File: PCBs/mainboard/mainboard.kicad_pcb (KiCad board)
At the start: 2 copper layers, 76.6 x 80 mm, 32 parts, among them J1 USB_C_Receptacle_USB2.0_16P, SW1 SW_Push_Dual, SW2 SW_Push_Dual, SW3 SW_Push_Dual, U3 ESP32-S3-WROOM-1

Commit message: Layouting pt.1
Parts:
- moved D5 76.5 mm to (83.2, 134.1)
- moved R3 74.3 mm to (83.2, 132.1), turned to 180 degrees
- moved D3 73.5 mm to (60.6, 109.9), turned to 135 degrees
- moved D4 72.3 mm to (60.6, 108.0), turned to -135 degrees
- moved C8 72.1 mm to (82.8, 77.7), turned to -45 degrees
- moved C3 71.2 mm to (83.2, 129.7), turned to 180 degrees
- moved R1 71.2 mm to (61.8, 106.1), turned to 0 degrees
- moved C2 70.5 mm to (83.8, 121.1), turned to 0 degrees
- moved R2 70.4 mm to (62.7, 112.0)
- moved D2 70.3 mm to (60.5, 112.1), turned to 135 degrees
- moved R8 69.8 mm to (61.8, 103.7), turned to 0 degrees
- moved U4 69.1 mm to (82.9, 125.2), turned to 0 degrees
- moved D1 68.9 mm to (63.3, 115.5)
- moved U2 68.7 mm to (109.5, 132.7)
- moved R6 68.4 mm to (82.1, 74.1), turned to 90 degrees
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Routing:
- net VCC_3V3: track 30.8 -> 229.9 mm, vias 0 -> 3
- net GPIO16: track 6.50 -> 63.2 mm, vias 0 -> 1
- net ESP_3V3: track 11.7 -> 54.8 mm, vias 0 -> 2
- net D-: track 0.00 -> 42.2 mm
- net D+: track 0.00 -> 41.3 mm
- net VCC_4V5: track 15.0 -> 45.9 mm, vias 0 -> 1
- net CHIP_PU: track 33.2 -> 46.1 mm, vias 0 -> 2
- net Net-(D1-A): track 0.00 -> 12.0 mm
- net VCC_5V: track 3.37 -> 14.2 mm
- net GPIO37: track 93.5 -> 102.6 mm
- net GPIO39: track 83.8 -> 92.7 mm
- net Net-(J1-CC2): track 0.00 -> 3.83 mm
- net Net-(J1-CC1): track 0.00 -> 3.05 mm
- net GPIO0: track 0.00 -> 3.03 mm
- net GPIO35: track 70.9 -> 72.8 mm
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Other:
- copper layers 2 -> 4
- board text added: "BOOT"
- board text removed: "Boot"

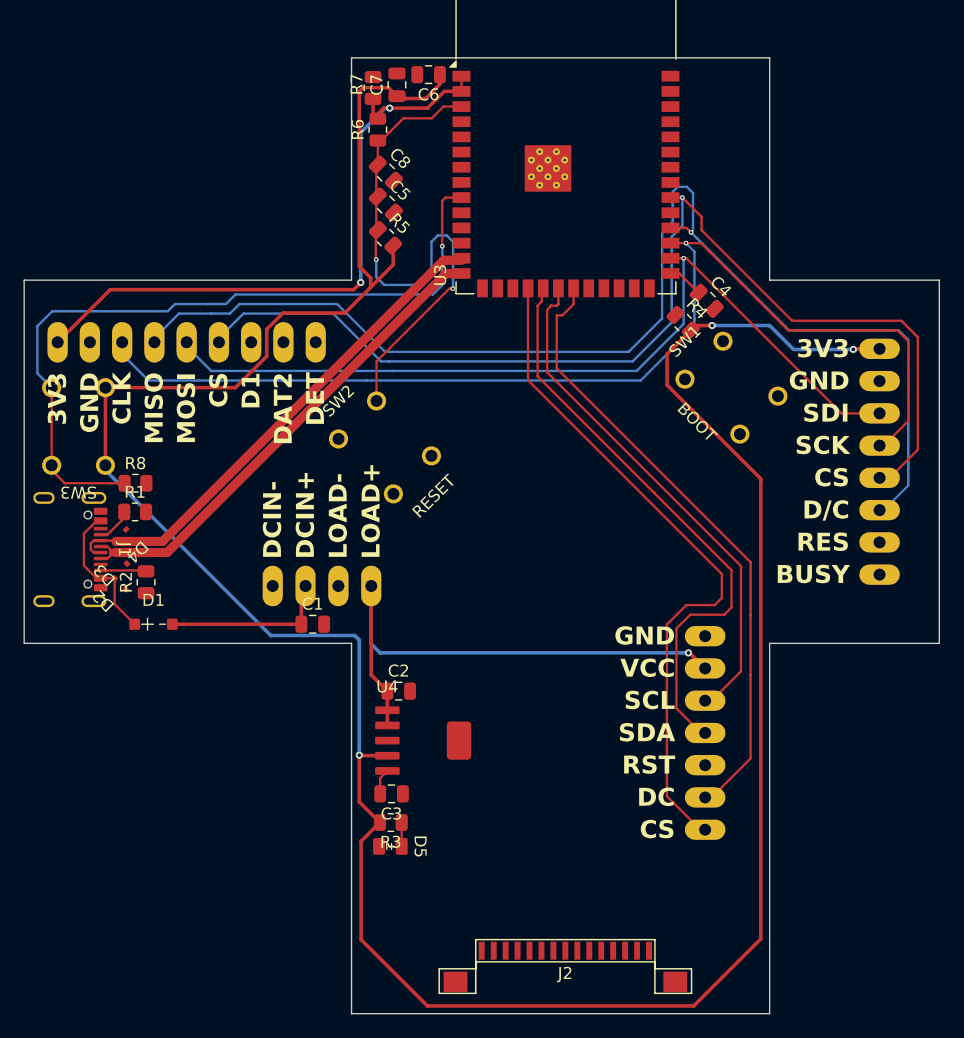
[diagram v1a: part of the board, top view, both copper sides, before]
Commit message: Routed peripherals
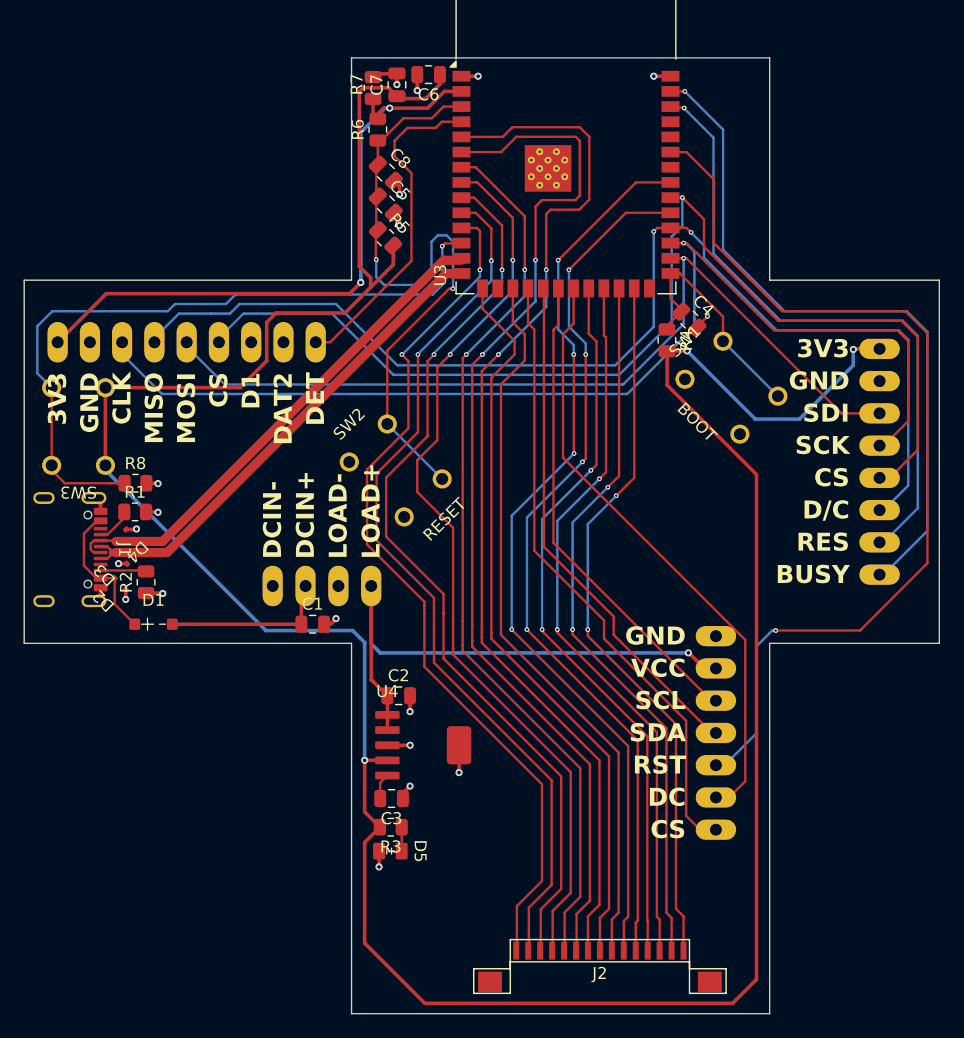
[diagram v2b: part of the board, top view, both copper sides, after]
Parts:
- moved J2 2.89 mm to (100.7, 142.8)
- moved C4 2.14 mm to (108.2, 90.0)
- moved SW2 2.13 mm to (83.6, 102.6)
- moved R4 2.01 mm to (106.3, 91.7), turned to -90 degrees
- moved U2 0.90 mm to (110.4, 132.7)
- moved C3 0.39 mm to (83.2, 130.1)
- moved D5 0.39 mm to (83.2, 134.5)
- moved R3 0.39 mm to (83.2, 132.5)
- moved C2 0.39 mm to (83.8, 121.5)
- moved U4 0.39 mm to (82.9, 125.6)
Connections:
- R8 pad 1: GPIO16 -> GPIO8
- SW3 pad 2: GPIO16 -> GPIO8
- SW3 pad 4: GPIO16 -> GPIO8
- U2 pad 3: GPIO48 -> GPIO42
- U3 pad 10: Column 3 -> Column 1
- U3 pad 11: Row 0 -> Column 0
- U3 pad 12: Column 10 -> GPIO8
- U3 pad 15: Column 2 -> Column 3
- U3 pad 17: Column 9 -> Column 4
- U3 pad 22: Column 8 -> Column 7
- U3 pad 23: Row 1 -> Column 8
- U3 pad 24: GPIO47 -> Column 9
- U3 pad 25: GPIO48 -> Column 10
- U3 pad 31: GPIO38 -> Column 6
- U3 pad 33: Column 6 -> Column 5
- U3 pad 35: Row 2 -> GPIO42
- U3 pad 38: Column 1 -> GPIO2
- U3 pad 39: Column 0 -> GPIO1
- U3 pad 4: Column 5 -> GPIO4
- U3 pad 5: Column 4 -> Row 3
- U3 pad 6: Row 3 -> Row 2
- U3 pad 7: GPIO7 -> Row 1
- U3 pad 8: Column 7 -> Row 0
- U3 pad 9: GPIO16 -> Column 2
- U5 pad 1: GPIO38 -> GPIO1
- U5 pad 2: GPIO47 -> GPIO2
- U6 pad 9: GPIO7 -> GPIO4
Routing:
- net Row 3: track 0.00 -> 89.1 mm, vias 0 -> 2
- net Row 2: track 0.00 -> 88.3 mm, vias 0 -> 2
- net GPIO42: track 0.00 -> 80.0 mm, vias 0 -> 1
- net Column 5: track 0.00 -> 76.8 mm, vias 0 -> 4
- net Column 2: track 0.00 -> 76.5 mm, vias 0 -> 2
- net Row 0: track 0.00 -> 76.2 mm, vias 0 -> 2
- net Row 1: track 0.00 -> 75.3 mm, vias 0 -> 2
- net Column 1: track 0.00 -> 74.4 mm, vias 0 -> 2
- net Column 6: track 0.00 -> 74.0 mm, vias 0 -> 4
- net Column 0: track 0.00 -> 73.2 mm, vias 0 -> 2
- net GPIO16: track 63.2 -> 0.00 mm, vias 1 -> 0
- net Column 3: track 0.00 -> 61.8 mm
- net Column 7: track 0.00 -> 61.3 mm, vias 0 -> 2
- net Column 4: track 0.00 -> 61.0 mm
- net Column 8: track 0.00 -> 60.8 mm, vias 0 -> 2
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- added copper zone on In1.Cu, net GND
- added copper zone on In2.Cu, net GND

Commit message: Verification
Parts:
- moved C7 2.94 mm to (86.4, 71.6), turned to 180 degrees
- moved R6 1.68 mm to (83.5, 75.0), turned to -45 degrees
- moved R5 1.24 mm to (83.2, 84.2)
- moved C5 1.09 mm to (83.4, 81.2)
- moved C8 0.93 mm to (83.5, 78.2)
- moved R7 0.67 mm to (82.4, 70.4), turned to 45 degrees
- moved R4 0.54 mm to (106.0, 92.2)
- moved C4 0.20 mm to (108.2, 90.2)
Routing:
- net VCC_3V3: track 235.0 -> 225.7 mm
- net ESP_3V3: track 53.3 -> 59.8 mm, vias 2 -> 3
- net GPIO13: track 51.9 -> 56.4 mm
- net CHIP_PU: track 54.5 -> 57.5 mm, vias 2 -> 4
- net GPIO4: track 27.7 -> 25.8 mm
- net GPIO0: track 20.0 -> 20.6 mm
- net GND: track 29.0 -> 29.4 mm, vias 19 -> 20
